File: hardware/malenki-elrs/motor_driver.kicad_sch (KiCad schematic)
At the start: 3 parts, among them J4 Conn_01x02_Male-Connector, U4 DRV8837DSGR

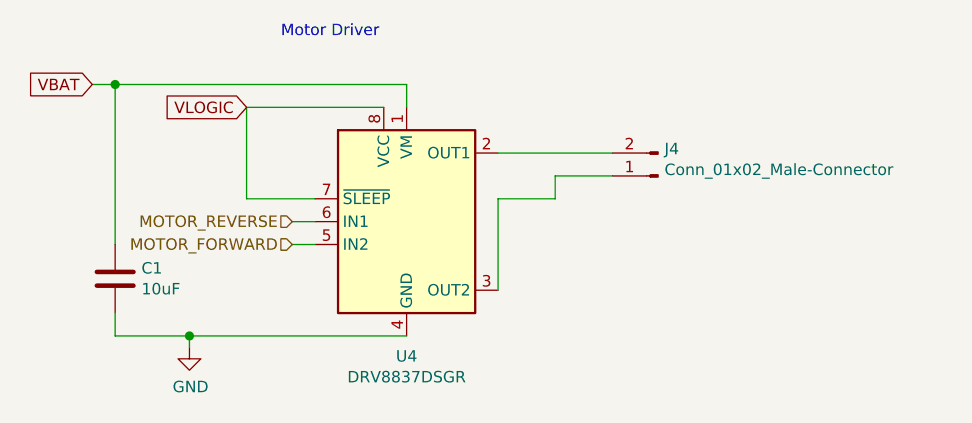
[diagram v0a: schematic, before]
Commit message: Adding elrs rf chip and esp32 micro controller.
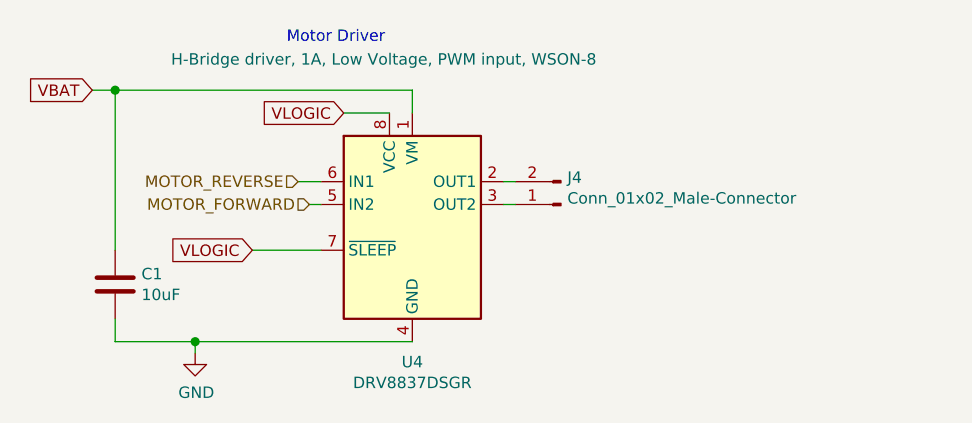
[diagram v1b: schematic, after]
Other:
- moved on the sheet: C1, J4, U4

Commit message: Completed preliminary schematics
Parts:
- renumbered C1 to C24
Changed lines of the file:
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@@
 		(in_pos_files yes)
 		(dnp no)
-		(property "Reference" "#PWR01"
+		(property "Reference" "#PWR028"
 			(at 123.19 118.11 0)
 			(hide yes)
@@
 			(project "malenki-elrs"
 				(path "/f41619e3-8cf2-4511-8a51-762d4de43197/159e78dd-19f3-45d1-a83d-5b1f96539c1f"
-					(reference "#PWR03")
+					(reference "#PWR029")
 					(unit 1)
 				)
 				(path "/f41619e3-8cf2-4511-8a51-762d4de43197/b339fba4-a8e4-4c66-ad9c-610bd968ae93"
-					(reference "#PWR01")
+					(reference "#PWR028")
 					(unit 1)
 				)
 				(path "/f41619e3-8cf2-4511-8a51-762d4de43197/ed035ea4-687d-4ec6-a6e6-057c20ae2a22"
-					(reference "#PWR08")
+					(reference "#PWR030")
 					(unit 1)
 				)
@@
 		(in_pos_files yes)
 		(dnp no)
-		(property "Reference" "C1"
+		(property "Reference" "C24"
 			(at 117.221 102.9716 0)
 			(show_name no)
@@
 			(project "malenki-elrs"
 				(path "/f41619e3-8cf2-4511-8a51-762d4de43197/159e78dd-19f3-45d1-a83d-5b1f96539c1f"
-					(reference "C5")
+					(reference "C25")
 					(unit 1)
 				)
 				(path "/f41619e3-8cf2-4511-8a51-762d4de43197/b339fba4-a8e4-4c66-ad9c-610bd968ae93"
-					(reference "C1")
+					(reference "C24")
 					(unit 1)
 				)
 				(path "/f41619e3-8cf2-4511-8a51-762d4de43197/ed035ea4-687d-4ec6-a6e6-057c20ae2a22"
-					(reference "C6")
+					(reference "C26")
 					(unit 1)
 				)

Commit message: Generated production files
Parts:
- C24: LCSC C96446 -> (none); LCSC Part # (none) -> C96446; Manufacturer Samsung -> (none)
- U4: LCSC C39159 -> (none); LCSC Part # (none) -> C39159; Manufacturer TI -> (none)
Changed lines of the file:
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@@
 			)
 		)
-		(property "LCSC" "C96446"
-			(at 114.3 104.14 0)
-			(hide yes)
-			(show_name no)
-			(do_not_autoplace no)
-			(effects
-				(font
-					(size 1.27 1.27)
-				)
-			)
-		)
-		(property "Manufacturer" "Samsung"
+		(property "LCSC Part #" "C96446"
 			(at 114.3 104.14 0)
 			(hide yes)
@@
 			)
 		)
-		(property "LCSC" "C39159"
+		(property "LCSC Part #" "C39159"
 			(at 147.32 97.79 0)
 			(hide yes)
@@
 			(at 147.32 97.79 0)
 			(hide yes)
-			(show_name no)
-			(do_not_autoplace no)
-			(effects
-				(font
-					(size 1.27 1.27)
-				)
-			)
-		)
-		(property "Manufacturer" "TI"
-			(at 147.32 97.79 0)
-			(hide yes)
